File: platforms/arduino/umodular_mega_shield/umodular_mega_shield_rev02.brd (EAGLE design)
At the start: 53.5 x 100 mm, 32 parts, among them IC1 23LC1024, IC2 74HC4050/CD4050, IC3 6N138, U1 ARDUINO-MEGA-SHIELD

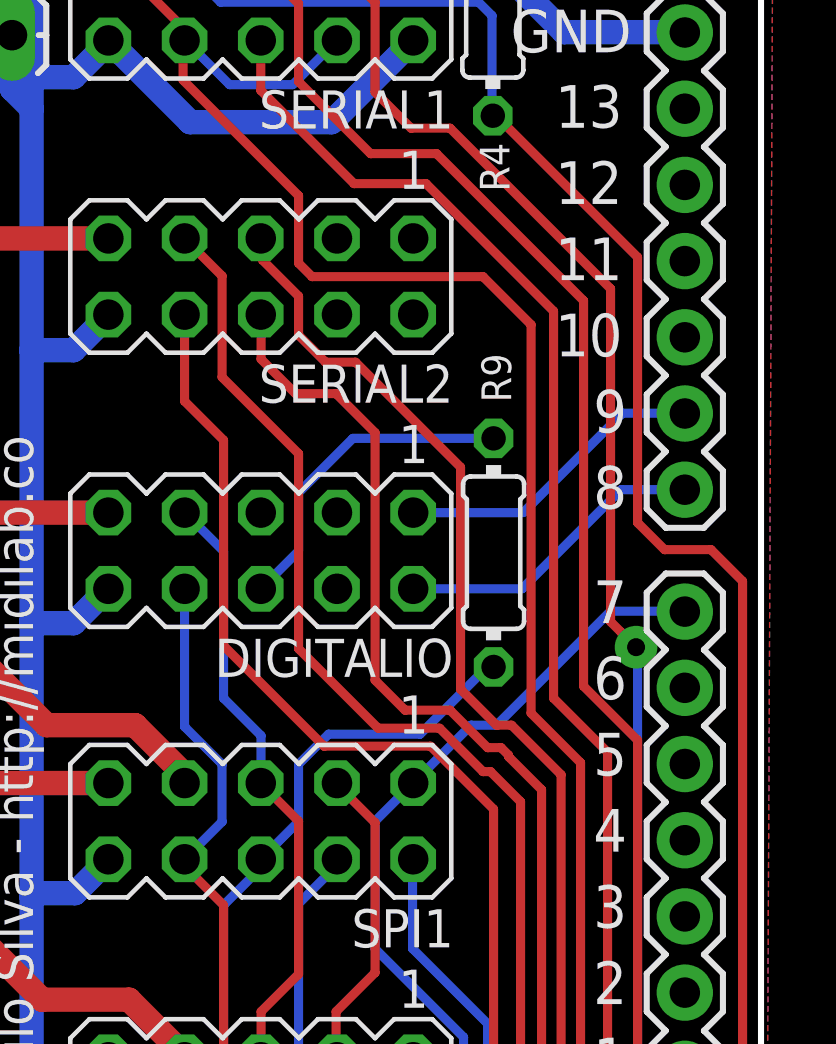
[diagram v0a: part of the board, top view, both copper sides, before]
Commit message: Change shift registers from SPI hardware based to Software implementation. Free the SPI bus for things more important(SDCARD and RAM)
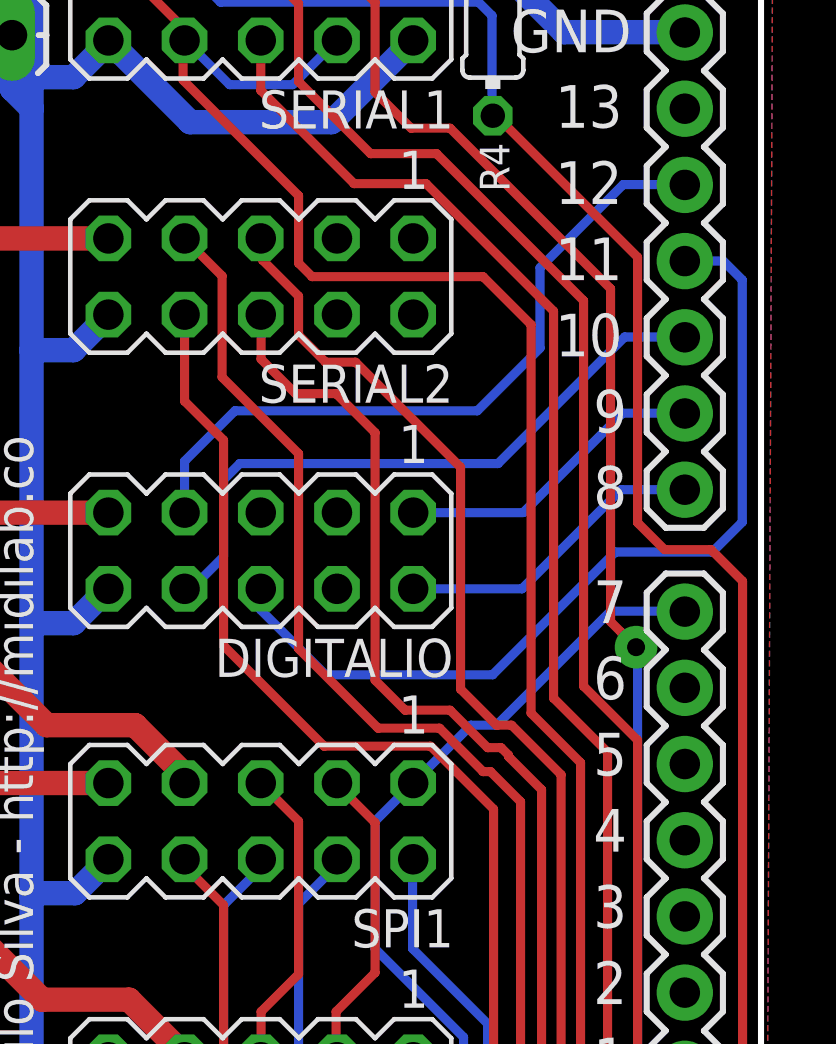
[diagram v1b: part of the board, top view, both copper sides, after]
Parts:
- removed R9: 2.2k, rcl:0204/7@1
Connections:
- net SPI_SS4 renamed LATCH_595
- net SPI_SS5 renamed LATCH_165
- removed net N$9: DIGITALIO.6, R9.2
- new net SR_CLOCK: DIGITALIO.7, U1.12
- new net SR_DATA_165: DIGITALIO.6, U1.11
- new net SR_DATA_595: DIGITALIO.8, U1.10
- net SPI_CLOCK: no longer DIGITALIO.7
- net SPI_MISO: no longer R9.1
- net SPI_MOSI: no longer DIGITALIO.8
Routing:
- net SR_DATA_165: track 0.00 -> 30.0 mm
- net SR_CLOCK: track 0.00 -> 23.8 mm
- net SR_DATA_595: track 0.00 -> 21.7 mm
- net SPI_MISO: track 83.6 -> 72.1 mm
- net N$9: track 11.0 -> 0.00 mm
- net SPI_CLOCK: track 80.5 -> 70.5 mm
- net SPI_MOSI: track 90.7 -> 80.6 mm
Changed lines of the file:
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@@
 <attribute name="VALUE" x="52.609" y="14.367" size="1.27" layer="27" ratio="10" rot="R180"/>
-</element>
-<element name="R9" library="rcl" package="0204/7@1" value="2.2k" x="44.55" y="58.45" smashed="yes" rot="R90">
-<attribute name="NAME" x="44.1454" y="65.09" size="0.9906" layer="25" ratio="10" rot="R270"/>
-<attribute name="VALUE" x="45.0326" y="56.8244" size="0.9906" layer="27" ratio="10" rot="R90"/>
 </element>
 <element name="POWER" library="SparkFun-Connectors" package="1X02_LOCK_LONGPADS" value="+5V" x="25.83" y="75.7" smashed="yes">
@@
 </signal>
 <signal name="SPI_CLOCK">
-<contactref element="DIGITALIO" pad="7"/>
 <contactref element="U1" pad="52"/>
 <contactref element="IC1" pad="6"/>
@@
 <wire x1="30.25" y1="12.95" x2="30.25" y2="13.775" width="0.3048" layer="1"/>
 <wire x1="30.25" y1="13.775" x2="30.265" y2="13.79" width="0.3048" layer="1"/>
-<wire x1="34.25" y1="59.785" x2="34.265" y2="59.785" width="0.3048" layer="16"/>
-<wire x1="34.265" y1="59.785" x2="35.55" y2="58.5" width="0.3048" layer="16"/>
-<wire x1="35.55" y1="58.5" x2="35.55" y2="53.6" width="0.3048" layer="16"/>
-<wire x1="35.55" y1="53.6" x2="36.8" y2="52.35" width="0.3048" layer="16"/>
-<wire x1="36.8" y1="52.35" x2="36.8" y2="50.78" width="0.3048" layer="16"/>
-<wire x1="36.8" y1="50.78" x2="36.79" y2="50.77" width="0.3048" layer="16"/>
 <wire x1="36.79" y1="50.77" x2="36.79" y2="50.76" width="0.3048" layer="1"/>
 <wire x1="36.79" y1="50.76" x2="38.05" y2="49.5" width="0.3048" layer="1"/>
@@
 <contactref element="U1" pad="50"/>
 <contactref element="IC1" pad="2"/>
-<contactref element="R9" pad="1"/>
 <contactref element="SPI2" pad="6"/>
 <contactref element="SPI3" pad="6"/>
@@
 <wire x1="13.55" y1="9.95" x2="14.15" y2="9.95" width="0.3048" layer="1"/>
 <wire x1="13.75" y1="10.35" x2="14.15" y2="9.95" width="0.3048" layer="16"/>
-<wire x1="44.55" y1="54.64" x2="44.34" y2="54.64" width="0.3048" layer="16"/>
-<wire x1="44.34" y1="54.64" x2="42.1" y2="52.4" width="0.3048" layer="16"/>
-<wire x1="42.1" y1="52.4" x2="39.05" y2="52.4" width="0.3048" layer="16"/>
-<wire x1="39.05" y1="52.4" x2="38.05" y2="51.4" width="0.3048" layer="16"/>
-<wire x1="38.05" y1="51.4" x2="38.05" y2="49.49" width="0.3048" layer="16"/>
-<wire x1="38.05" y1="49.49" x2="36.79" y2="48.23" width="0.3048" layer="16"/>
 <wire x1="36.79" y1="48.23" x2="36.79" y2="47.94" width="0.3048" layer="16"/>
 <wire x1="36.79" y1="47.94" x2="35.55" y2="46.7" width="0.3048" layer="16"/>
@@
 </signal>
 <signal name="SPI_MOSI">
-<contactref element="DIGITALIO" pad="8"/>
 <contactref element="U1" pad="51"/>
 <contactref element="IC1" pad="5"/>
@@
 <wire x1="25.2" y1="13" x2="25.2" y2="13.775" width="0.3048" layer="1"/>
 <wire x1="25.2" y1="13.775" x2="25.185" y2="13.79" width="0.3048" layer="1"/>
-<wire x1="34.25" y1="57.245" x2="34.25" y2="52.65" width="0.3048" layer="16"/>
-<wire x1="34.25" y1="52.65" x2="35.5" y2="51.4" width="0.3048" layer="16"/>
-<wire x1="35.5" y1="51.4" x2="35.5" y2="49.48" width="0.3048" layer="16"/>
-<wire x1="35.5" y1="49.48" x2="34.25" y2="48.23" width="0.3048" layer="16"/>
 <wire x1="34.25" y1="48.23" x2="34.25" y2="48" width="0.3048" layer="1"/>
 <wire x1="34.25" y1="48" x2="35.55" y2="46.7" width="0.3048" layer="1"/>
@@
 <wire x1="27.15" y1="23.45" x2="27.805" y2="23.45" width="0.3048" layer="1"/>
 <wire x1="27.805" y1="23.45" x2="34.21" y2="29.855" width="0.3048" layer="1"/>
-</signal>
-<signal name="SPI_SS5">
-<contactref element="U1" pad="9"/>
-<contactref element="DIGITALIO" pad="1"/>
-<wire x1="41.87" y1="59.785" x2="45.535" y2="59.785" width="0.3048" layer="16"/>
-<wire x1="45.535" y1="59.785" x2="48.85" y2="63.1" width="0.3048" layer="16"/>
-<wire x1="48.85" y1="63.1" x2="50.914" y2="63.1" width="0.3048" layer="16"/>
-<wire x1="50.914" y1="63.1" x2="50.925" y2="63.089" width="0.3048" layer="16"/>
 </signal>
 <signal name="SPI_SS3">
@@
 <wire x1="47.05" y1="14.15" x2="47.05" y2="24.6" width="0.3048" layer="1"/>
 <wire x1="47.05" y1="24.6" x2="43.55" y2="28.1" width="0.3048" layer="1"/>
-</signal>
-<signal name="SPI_SS4">
-<contactref element="U1" pad="8"/>
-<contactref element="DIGITALIO" pad="2"/>
-<wire x1="41.87" y1="57.245" x2="45.495" y2="57.245" width="0.3048" layer="16"/>
-<wire x1="45.495" y1="57.245" x2="48.8" y2="60.55" width="0.3048" layer="16"/>
-<wire x1="48.8" y1="60.55" x2="50.924" y2="60.55" width="0.3048" layer="16"/>
-<wire x1="50.924" y1="60.55" x2="50.925" y2="60.549" width="0.3048" layer="16"/>
 </signal>
 <signal name="SPI_SS2">
@@
 <wire x1="41.85" y1="29.835" x2="41.83" y2="29.855" width="0.3048" layer="16"/>
 </signal>
-<signal name="N$9">
-<contactref element="DIGITALIO" pad="6"/>
-<contactref element="R9" pad="2"/>
-<wire x1="44.55" y1="62.26" x2="39.86" y2="62.26" width="0.3048" layer="16"/>
-<wire x1="39.86" y1="62.26" x2="38.05" y2="60.45" width="0.3048" layer="16"/>
-<wire x1="38.05" y1="60.45" x2="38.05" y2="58.505" width="0.3048" layer="16"/>
-<wire x1="38.05" y1="58.505" x2="36.79" y2="57.245" width="0.3048" layer="16"/>
-</signal>
 <signal name="UART_TX3_3_3V">
 <contactref element="SERIAL1" pad="3"/>
@@
 <wire x1="49.3" y1="55.3" x2="48.8" y2="55.8" width="0.3048" layer="1"/>
 </signal>
+<signal name="SR_CLOCK">
+<contactref element="DIGITALIO" pad="7"/>
+<contactref element="U1" pad="12"/>
+<wire x1="34.25" y1="59.785" x2="34.25" y2="61.5" width="0.3048" layer="16"/>
+<wire x1="34.25" y1="61.5" x2="35.93" y2="63.18" width="0.3048" layer="16"/>
+<wire x1="35.93" y1="63.18" x2="44.01" y2="63.18" width="0.3048" layer="16"/>
+<wire x1="44.01" y1="63.18" x2="46.1" y2="65.27" width="0.3048" layer="16"/>
+<wire x1="46.1" y1="65.27" x2="46.1" y2="67.95" width="0.3048" layer="16"/>
+<wire x1="46.1" y1="67.95" x2="48.87" y2="70.72" width="0.3048" layer="16"/>
+<wire x1="48.87" y1="70.72" x2="50.914" y2="70.72" width="0.3048" layer="16"/>
+<wire x1="50.914" y1="70.72" x2="50.925" y2="70.709" width="0.3048" layer="16"/>
+</signal>
+<signal name="SR_DATA_165">
+<contactref element="DIGITALIO" pad="6"/>
+<contactref element="U1" pad="11"/>
+<wire x1="36.79" y1="57.245" x2="36.79" y2="56.54" width="0.3048" layer="16"/>
+<wire x1="36.79" y1="56.54" x2="38.95" y2="54.38" width="0.3048" layer="16"/>
+<wire x1="38.95" y1="54.38" x2="44.52" y2="54.38" width="0.3048" layer="16"/>
+<wire x1="44.52" y1="54.38" x2="48.61" y2="58.47" width="0.3048" layer="16"/>
+<wire x1="48.61" y1="58.47" x2="51.84" y2="58.47" width="0.3048" layer="16"/>
+<wire x1="51.84" y1="58.47" x2="52.84" y2="59.47" width="0.3048" layer="16"/>
+<wire x1="52.84" y1="59.47" x2="52.84" y2="67.54" width="0.3048" layer="16"/>
+<wire x1="52.84" y1="67.54" x2="52.21" y2="68.17" width="0.3048" layer="16"/>
+<wire x1="52.21" y1="68.17" x2="50.926" y2="68.17" width="0.3048" layer="16"/>
+<wire x1="50.926" y1="68.17" x2="50.925" y2="68.169" width="0.3048" layer="16"/>
+</signal>
+<signal name="SR_DATA_595">
+<contactref element="DIGITALIO" pad="8"/>
+<contactref element="U1" pad="10"/>
+<wire x1="34.25" y1="57.245" x2="34.475" y2="57.245" width="0.3048" layer="16"/>
+<wire x1="34.475" y1="57.245" x2="35.55" y2="58.32" width="0.3048" layer="16"/>
+<wire x1="35.55" y1="58.32" x2="35.55" y2="60.88" width="0.3048" layer="16"/>
+<wire x1="35.55" y1="60.88" x2="36.09" y2="61.42" width="0.3048" layer="16"/>
+<wire x1="36.09" y1="61.42" x2="44.7" y2="61.42" width="0.3048" layer="16"/>
+<wire x1="44.7" y1="61.42" x2="48.92" y2="65.64" width="0.3048" layer="16"/>
+<wire x1="48.92" y1="65.64" x2="50.914" y2="65.64" width="0.3048" layer="16"/>
+<wire x1="50.914" y1="65.64" x2="50.925" y2="65.629" width="0.3048" layer="16"/>
+</signal>
+<signal name="LATCH_165">
+<contactref element="DIGITALIO" pad="1"/>
+<contactref element="U1" pad="9"/>
+<wire x1="45.535" y1="59.785" x2="48.85" y2="63.1" width="0.3048" layer="16"/>
+<wire x1="48.85" y1="63.1" x2="50.914" y2="63.1" width="0.3048" layer="16"/>
+<wire x1="50.914" y1="63.1" x2="50.925" y2="63.089" width="0.3048" layer="16"/>
+<wire x1="45.535" y1="59.785" x2="41.87" y2="59.785" width="0.3048" layer="16"/>
+</signal>
+<signal name="LATCH_595">
+<contactref element="DIGITALIO" pad="2"/>
+<contactref element="U1" pad="8"/>
+<wire x1="45.495" y1="57.245" x2="48.8" y2="60.55" width="0.3048" layer="16"/>
+<wire x1="48.8" y1="60.55" x2="50.924" y2="60.55" width="0.3048" layer="16"/>
+<wire x1="50.924" y1="60.55" x2="50.925" y2="60.549" width="0.3048" layer="16"/>
+<wire x1="45.495" y1="57.245" x2="41.87" y2="57.245" width="0.3048" layer="16"/>
+</signal>
 </signals>
